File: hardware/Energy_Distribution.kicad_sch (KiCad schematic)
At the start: 23 parts, among them J15 53398-0271, J16 533980671, J17 533980671, J18 53398-0271, U17 NVTFS5116PLTAG, U18 NVTFS5116PLTAG, U19 INA199C3DCKR, U21 LMV321RIYLT, U39 NVTFS5116PLTAG, U40 NVTFS5116PLTAG

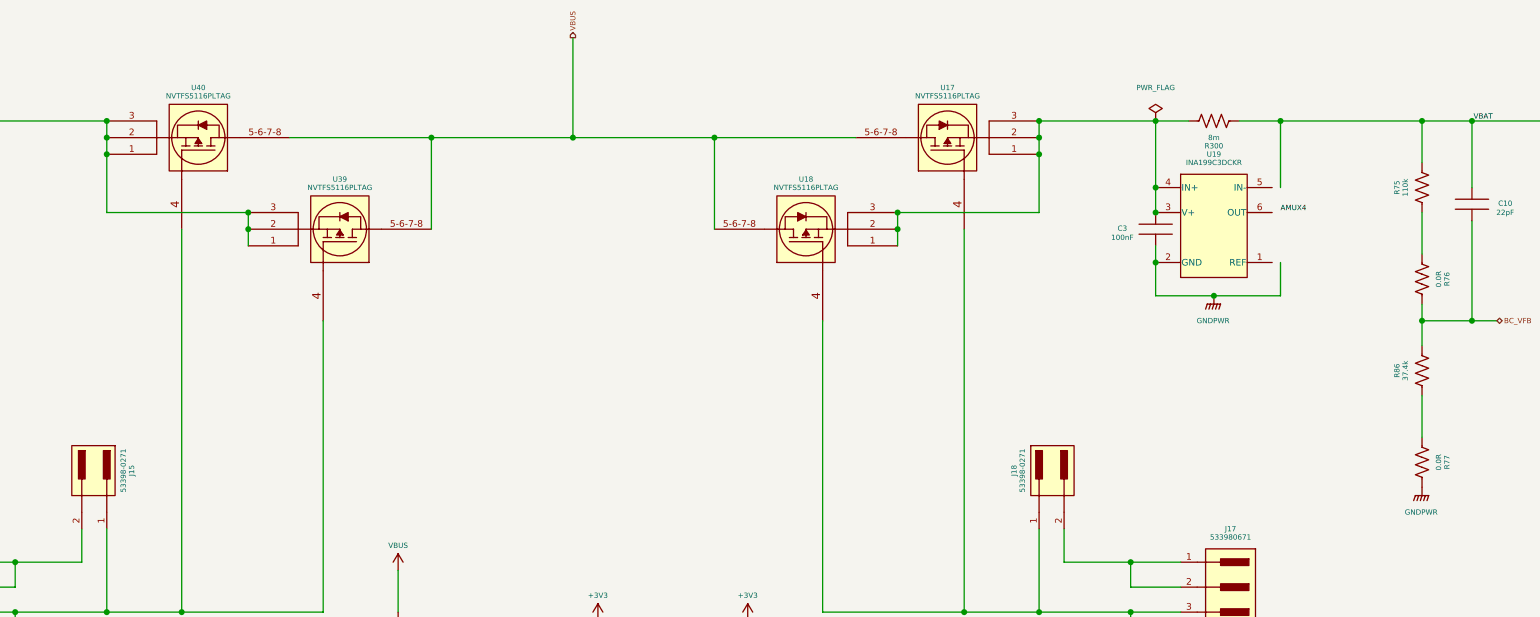
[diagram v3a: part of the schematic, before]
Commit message: hardware: Minor improvements to the schematics
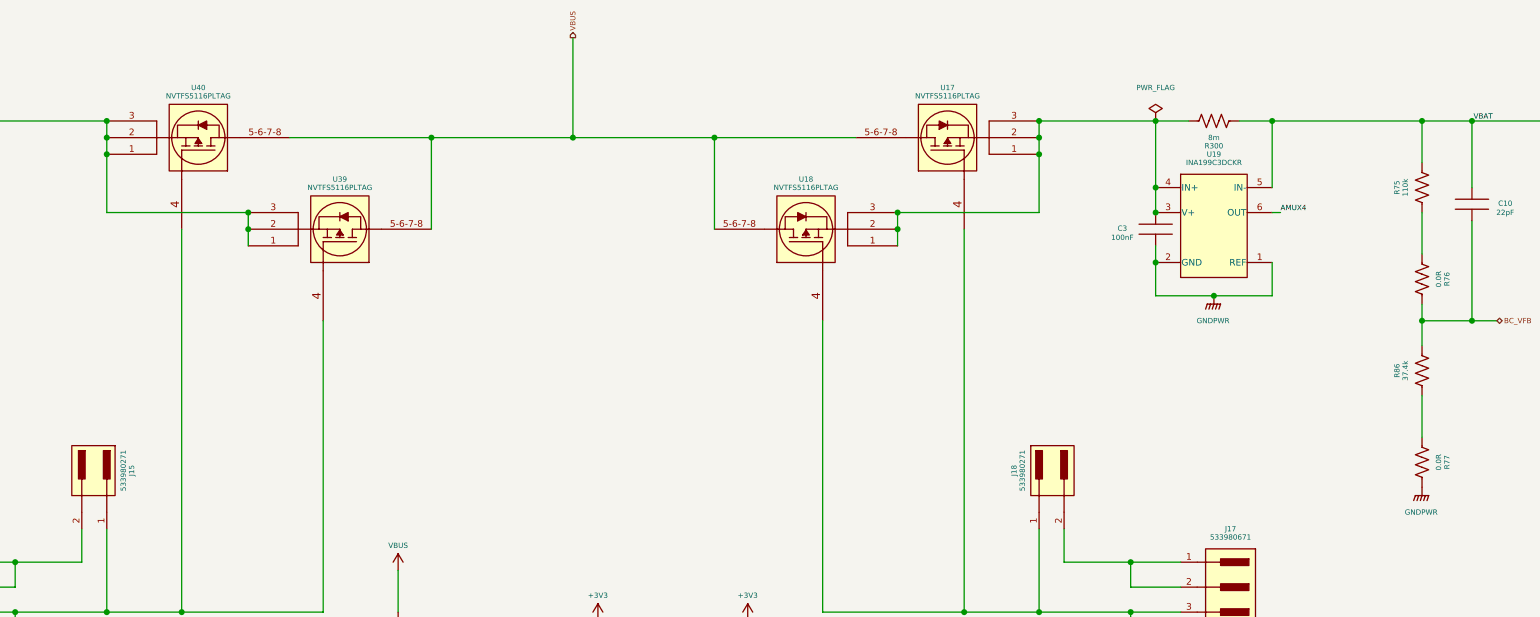
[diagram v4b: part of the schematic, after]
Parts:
- J15, J18: value 53398-0271 -> 533980271; MPN (none) -> 533980271; Manufacturer (none) -> Molex; Package (none) -> PicoBlade (2P); category Conn -> (none); contact material Tin -> (none); current rating 1A -> (none); device class L1 Connectors -> (none); device class L2 Headers and Wire Housings -> (none); device class L3 unset -> (none); digikey description CONN HEADER 2POS 1.25MM VERT SMD -> (none); digikey part number WM7606CT-ND -> (none); height 4.9mm -> (none); is connector yes -> (none); is male yes -> (none); lead free yes -> (none); library id bd646e8792f35d91 -> (none); manufacturer Molex -> (none); mouser description Conn Shrouded Header HDR 2 POS 1.25mm Solder ST SMD PicoBla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 -> (none); mouser part number 538-53398-0271 -> (none); number of contacts 2 -> (none); number of rows 1 -> (none); package HDR2 -> (none); rohs yes -> (none); standoff height 0.05mm -> (none); temperature range high +85°C -> (none); temperature range low -40°C -> (none); voltage rating 125V -> (none)
- R75: MPN (none) -> CRCW0603110KFKEAHP; Manufacturer (none) -> Vishay; Package (none) -> SMD 0603
- R86: MPN (none) -> CRCW060337K4FKEAHP; Manufacturer (none) -> Vishay; Package (none) -> SMD 0603
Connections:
- net AMUX4: now also U19.6 (OUT)
- net GNDPWR: now also U19.1 (REF)
- net VBAT: now also U19.5 (IN-)

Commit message: hardware: Minor modifications for the upcoming release
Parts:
- TP2: MPN N/A -> S2761-46R; Manufacturer N/A -> Harwin; Package N/A -> Non-standard
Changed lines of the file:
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@@
       (effects (font (size 1.27 1.27)) hide)
     )
-    (property "Datasheet" "N/A" (at 140.97 185.42 0)
+    (property "Datasheet" "https://br.mouser.com/datasheet/2/181/S2761R-1291319.pdf" (at 140.97 185.42 0)
       (effects (font (size 1.27 1.27)) hide)
     )
-    (property "MPN" "N/A" (at 143.51 185.42 0)
+    (property "MPN" "S2761-46R" (at 143.51 185.42 0)
       (effects (font (size 1.27 1.27)) hide)
     )
-    (property "Package" "N/A" (at 146.05 185.42 0)
+    (property "Package" "Non-standard" (at 146.05 185.42 0)
       (effects (font (size 1.27 1.27)) hide)
     )
-    (property "Manufacturer" "N/A" (at 148.59 185.42 0)
+    (property "Manufacturer" "Harwin" (at 148.59 185.42 0)
       (effects (font (size 1.27 1.27)) hide)
     )

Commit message: hardware: update schematic and layout projects
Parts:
- removed J15, J18: 533980271, footprints:533980271, symbol 533980271:53398-0271
- removed J16, J17: 533980671, footprints:533980671, symbol 533980671:53398-0671
- added J10, J18: 532610271, footprints:532610271, symbol 532610271:532610271
- added J17, J9: 532610671, footprints:532610671, symbol 532610671:532610671
- R76, R77: value 0.0R -> 0R
- renumbered C3 to C41, C9 to C95, C10 to C97, R29 to R112, R30 to R113, R305 to R114, R300 to R116, R305 to R57, TP2 to TP6, U21 to U37
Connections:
- net VBAT: now also J10.2, J17.1, J17.2, J18.2, J9.1, J9.2
- net at U17.4, U18.4: now also J17.3, J17.4, J18.1
- net at U39.4, U40.4: now also J10.1, J9.3, J9.4
- net at R57.1: now also J17.5, J17.6
- net at R114.2: now also J9.5, J9.6
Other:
- moved on the sheet: C41, C95, C97, R112, R113, R114, R116, R57, R75, R76, R77, R86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
